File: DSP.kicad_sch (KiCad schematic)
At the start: 26 parts, among them J2 Conn_01x04, J3 Conn_01x04, J4 MEM2067-02-180-00-A_REVB, J6 Conn_01x04, U4 STM32F401RBTx, U5 23K256, Y1 16MHz

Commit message: modifications for rev 3
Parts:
- removed C28: 100n, Capacitor_SMD:C_0603_1608Metric_Pad1.08x0.95mm_HandSolder, symbol Device:C_Small
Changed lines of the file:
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@@
 (kicad_sch (version 20230121) (generator eeschema)
   (paper "A4")
-  (junction (at 53.34 154.94) (diameter 0) (color 0 0 0 0)
-  )
   (junction (at 114.3 34.29) (diameter 0) (color 0 0 0 0)
   )
@@
   (junction (at 167.64 34.29) (diameter 0) (color 0 0 0 0)
   )
+  (junction (at 67.31 177.8) (diameter 0) (color 0 0 0 0)
+  )
   (junction (at 140.97 90.17) (diameter 0) (color 0 0 0 0)
   )
@@
   (junction (at 185.42 110.49) (diameter 0) (color 0 0 0 0)
   )
-  (junction (at 53.34 177.8) (diameter 0) (color 0 0 0 0)
-  )
   (junction (at 111.76 128.27) (diameter 0) (color 0 0 0 0)
-  )
-  (junction (at 53.34 172.72) (diameter 0) (color 0 0 0 0)
   )
   (junction (at 66.04 87.63) (diameter 0) (color 0 0 0 0)
@@
     (stroke (width 0) (type default))
   )
-  (wire (pts (xy 53.34 167.64) (xy 53.34 172.72))
-    (stroke (width 0) (type default))
-  )
   (wire (pts (xy 111.76 125.73) (xy 111.76 128.27))
     (stroke (width 0) (type default))
@@
     (stroke (width 0) (type default))
   )
+  (wire (pts (xy 67.31 152.4) (xy 67.31 154.94))
+    (stroke (width 0) (type default))
+  )
   (wire (pts (xy 60.96 74.93) (xy 66.04 74.93))
     (stroke (width 0) (type default))
@@
     (stroke (width 0) (type default))
   )
+  (wire (pts (xy 67.31 154.94) (xy 69.85 154.94))
+    (stroke (width 0) (type default))
+  )
   (wire (pts (xy 185.42 118.11) (xy 185.42 120.65))
     (stroke (width 0) (type default))
@@
     (stroke (width 0) (type default))
   )
-  (wire (pts (xy 53.34 177.8) (xy 53.34 179.07))
-    (stroke (width 0) (type default))
-  )
   (wire (pts (xy 157.48 43.18) (xy 157.48 44.45))
     (stroke (width 0) (type default))
@@
     (stroke (width 0) (type default))
   )
-  (wire (pts (xy 53.34 177.8) (xy 69.85 177.8))
-    (stroke (width 0) (type default))
-  )
   (wire (pts (xy 172.72 34.29) (xy 177.8 34.29))
     (stroke (width 0) (type default))
@@
     (stroke (width 0) (type default))
   )
+  (wire (pts (xy 67.31 172.72) (xy 67.31 177.8))
+    (stroke (width 0) (type default))
+  )
   (wire (pts (xy 214.63 130.81) (xy 215.9 130.81))
     (stroke (width 0) (type default))
@@
     (stroke (width 0) (type default))
   )
+  (wire (pts (xy 67.31 177.8) (xy 67.31 180.34))
+    (stroke (width 0) (type default))
+  )
   (wire (pts (xy 111.76 128.27) (xy 114.3 128.27))
     (stroke (width 0) (type default))
@@
     (stroke (width 0) (type default))
   )
+  (wire (pts (xy 69.85 172.72) (xy 67.31 172.72))
+    (stroke (width 0) (type default))
+  )
   (wire (pts (xy 142.24 90.17) (xy 140.97 90.17))
     (stroke (width 0) (type default))
@@
     (stroke (width 0) (type default))
   )
+  (wire (pts (xy 67.31 177.8) (xy 69.85 177.8))
+    (stroke (width 0) (type default))
+  )
   (wire (pts (xy 140.97 96.52) (xy 140.97 97.79))
     (stroke (width 0) (type default))
@@
     (stroke (width 0) (type default))
   )
-  (wire (pts (xy 53.34 172.72) (xy 53.34 177.8))
-    (stroke (width 0) (type default))
-  )
   (wire (pts (xy 54.61 34.29) (xy 54.61 36.83))
     (stroke (width 0) (type default))
@@
     (stroke (width 0) (type default))
   )
-  (wire (pts (xy 53.34 172.72) (xy 69.85 172.72))
-    (stroke (width 0) (type default))
-  )
   (wire (pts (xy 182.88 38.1) (xy 182.88 34.29))
     (stroke (width 0) (type default))
@@
     (stroke (width 0) (type default))
   )
-  (wire (pts (xy 53.34 154.94) (xy 69.85 154.94))
-    (stroke (width 0) (type default))
-  )
   (wire (pts (xy 172.72 38.1) (xy 172.72 34.29))
     (stroke (width 0) (type default))
@@
     (stroke (width 0) (type default))
   )
-  (wire (pts (xy 53.34 152.4) (xy 53.34 154.94))
-    (stroke (width 0) (type default))
-  )
   (wire (pts (xy 214.63 123.19) (xy 215.9 123.19))
     (stroke (width 0) (type default))
@@
   )
   (wire (pts (xy 119.38 34.29) (xy 119.38 36.83))
-    (stroke (width 0) (type default))
-  )
-  (wire (pts (xy 53.34 154.94) (xy 53.34 162.56))
     (stroke (width 0) (type default))
   )
@@
     )
   )
-  (symbol (lib_id "power:GND") (at 53.34 179.07 0) (unit 1)
+  (symbol (lib_id "power:GND") (at 67.31 180.34 0) (unit 1)
     (in_bom yes) (on_board yes) (dnp no)
-    (property "Reference" "#PWR056" (at 53.34 185.42 0)
-      (effects (font (size 1.27 1.27)) hide)
-    )
-    (property "Value" "GND" (at 53.34 182.88 0)
-      (effects (font (size 1.27 1.27)))
-    )
-    (property "Footprint" "" (at 53.34 179.07 0)
-      (effects (font (size 1.27 1.27)) hide)
-    )
-    (property "Datasheet" "" (at 53.34 179.07 0)
+    (property "Reference" "#PWR056" (at 67.31 186.69 0)
+      (effects (font (size 1.27 1.27)) hide)
+    )
+    (property "Value" "GND" (at 67.31 184.15 0)
+      (effects (font (size 1.27 1.27)))
+    )
+    (property "Footprint" "" (at 67.31 180.34 0)
+      (effects (font (size 1.27 1.27)) hide)
+    )
+    (property "Datasheet" "" (at 67.31 180.34 0)
       (effects (font (size 1.27 1.27)) hide)
     )
@@
         (path "/e63e39d7-6ac0-4ffd-8aa3-1841a4541b55/65c41d2a-7921-40f6-8a66-43d43155f96a"
           (reference "#PWR035") (unit 1)
-        )
-      )
-    )
-  )
-  (symbol (lib_id "Device:C_Small") (at 53.34 165.1 0) (unit 1)
-    (in_bom yes) (on_board yes) (dnp no)
-    (property "Reference" "C28" (at 54.61 163.83 0)
-      (effects (font (size 1.27 1.27)) (justify left))
-    )
-    (property "Value" "100n" (at 54.61 166.37 0)
-      (effects (font (size 1.27 1.27)) (justify left))
-    )
-    (property "Footprint" "Capacitor_SMD:C_0603_1608Metric_Pad1.08x0.95mm_HandSolder" (at 53.34 165.1 0)
-      (effects (font (size 1.27 1.27)) hide)
-    )
-    (property "Datasheet" "~" (at 53.34 165.1 0)
-      (effects (font (size 1.27 1.27)) hide)
-    )
-    (pin "1")
-    (pin "2")
-    (instances
-      (project "Apollo - DSP"
-        (path "/e63e39d7-6ac0-4ffd-8aa3-1841a4541b55/65c41d2a-7921-40f6-8a66-43d43155f96a"
-          (reference "C28") (unit 1)
         )
       )
@@
     )
   )
-  (symbol (lib_id "power:+3.3V") (at 53.34 152.4 0) (unit 1)
-    (in_bom yes) (on_board yes) (dnp no) (fields_autoplaced)
-    (property "Reference" "#PWR055" (at 53.34 156.21 0)
-      (effects (font (size 1.27 1.27)) hide)
-    )
-    (property "Value" "+3.3V" (at 53.34 147.32 0)
-      (effects (font (size 1.27 1.27)))
-    )
-    (property "Footprint" "" (at 53.34 152.4 0)
-      (effects (font (size 1.27 1.27)) hide)
-    )
-    (property "Datasheet" "" (at 53.34 152.4 0)
-      (effects (font (size 1.27 1.27)) hide)
-    )
+  (symbol (lib_id "power:+3.3V") (at 67.31 152.4 0) (unit 1)
+    (in_bom yes) (on_board yes) (dnp no) (fields_autoplaced)
+    (property "Reference" "#PWR055" (at 67.31 156.21 0)
+      (effects (font (size 1.27 1.27)) hide)
+    )
+    (property "Value" "+3.3V" (at 67.31 147.32 0)
+      (effects (font (size 1.27 1.27)))
+    )
+    (property "Footprint" "" (at 67.31 152.4 0)
+      (effects (font (size 1.27 1.27)) hide)
+    )
+    (property "Datasheet" "" (at 67.31 152.4 0)
+      (effects (font (size 1.27 1.27)) hide)
+    )

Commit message: ready for order
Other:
- moved on the sheet: R?
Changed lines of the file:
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@@
   (junction (at 185.42 110.49) (diameter 0) (color 0 0 0 0)
+  )
+  (junction (at 82.55 46.99) (diameter 0) (color 0 0 0 0)
   )
   (junction (at 111.76 128.27) (diameter 0) (color 0 0 0 0)
@@
     (stroke (width 0) (type default))
   )
-  (wire (pts (xy 36.83 40.64) (xy 39.37 40.64))
+  (wire (pts (xy 82.55 46.99) (xy 81.28 46.99))
     (stroke (width 0) (type default))
   )
@@
     (stroke (width 0) (type default))
   )
-  (wire (pts (xy 36.83 43.18) (xy 36.83 40.64))
+  (wire (pts (xy 82.55 49.53) (xy 82.55 46.99))
     (stroke (width 0) (type default))
   )
@@
     (stroke (width 0) (type default))
   )
+  (wire (pts (xy 82.55 46.99) (xy 96.52 46.99))
+    (stroke (width 0) (type default))
+  )
   (wire (pts (xy 54.61 36.83) (xy 60.96 36.83))
     (stroke (width 0) (type default))
@@
     (stroke (width 0) (type default))
   )
-  (wire (pts (xy 36.83 48.26) (xy 36.83 49.53))
+  (wire (pts (xy 82.55 54.61) (xy 82.55 55.88))
     (stroke (width 0) (type default))
   )
@@
     (stroke (width 0) (type default))
   )
-  (global_label "BOOT0" (shape input) (at 39.37 40.64 0) (fields_autoplaced)
-    (effects (font (size 1 1)) (justify left))
-    (property "Intersheetrefs" "${INTERSHEET_REFS}" (at 46.0795 40.5775 0)
-      (effects (font (size 1 1)) (justify left) hide)
-    )
-  )
-  (global_label "BOOT0" (shape input) (at 96.52 46.99 180) (fields_autoplaced)
+  (global_label "BOOT0" (shape input) (at 81.28 46.99 180) (fields_autoplaced)
     (effects (font (size 1 1)) (justify right))
-    (property "Intersheetrefs" "${INTERSHEET_REFS}" (at 89.8105 46.9275 0)
+    (property "Intersheetrefs" "${INTERSHEET_REFS}" (at 74.1202 46.99 0)
       (effects (font (size 1 1)) (justify right) hide)
     )
@@
     )
   )
-  (symbol (lib_id "power:GND") (at 36.83 49.53 0) (unit 1)
-    (in_bom yes) (on_board yes) (dnp no) (fields_autoplaced)
-    (property "Reference" "#PWR?" (at 36.83 55.88 0)
-      (effects (font (size 1.27 1.27)) hide)
-    )
-    (property "Value" "GND" (at 36.83 54.61 0)
-      (effects (font (size 1.27 1.27)))
-    )
-    (property "Footprint" "" (at 36.83 49.53 0)
-      (effects (font (size 1.27 1.27)) hide)
-    )
-    (property "Datasheet" "" (at 36.83 49.53 0)
+  (symbol (lib_id "power:GND") (at 82.55 55.88 0) (unit 1)
+    (in_bom yes) (on_board yes) (dnp no)
+    (property "Reference" "#PWR?" (at 82.55 62.23 0)
+      (effects (font (size 1.27 1.27)) hide)
+    )
+    (property "Value" "GND" (at 82.55 59.69 0)
+      (effects (font (size 1.27 1.27)))
+    )
+    (property "Footprint" "" (at 82.55 55.88 0)
+      (effects (font (size 1.27 1.27)) hide)
+    )
+    (property "Datasheet" "" (at 82.55 55.88 0)
       (effects (font (size 1.27 1.27)) hide)
     )
@@
     )
   )
-  (symbol (lib_id "Device:R_Small") (at 36.83 45.72 0) (unit 1)
-    (in_bom yes) (on_board yes) (dnp no)
-    (property "Reference" "R?" (at 38.1 44.45 0)
-      (effects (font (size 1.27 1.27)) (justify left))
-    )
-    (property "Value" "10k" (at 38.1 46.99 0)
-      (effects (font (size 1.27 1.27)) (justify left))
-    )
-    (property "Footprint" "Resistor_SMD:R_0603_1608Metric_Pad0.98x0.95mm_HandSolder" (at 36.83 45.72 0)
-      (effects (font (size 1.27 1.27)) hide)
-    )
-    (property "Datasheet" "~" (at 36.83 45.72 0)
-      (effects (font (size 1.27 1.27)) hide)
-    )
+  (symbol (lib_id "Device:R_Small") (at 82.55 52.07 0) (unit 1)
+    (in_bom yes) (on_board yes) (dnp no)
+    (property "Reference" "R?" (at 83.82 50.8 0)
+      (effects (font (size 1.27 1.27)) (justify left))
+    )
+    (property "Value" "10k" (at 83.82 53.34 0)
+      (effects (font (size 1.27 1.27)) (justify left))
+    )
+    (property "Footprint" "Resistor_SMD:R_0603_1608Metric_Pad0.98x0.95mm_HandSolder" (at 82.55 52.07 0)
+      (effects (font (size 1.27 1.27)) hide)
+    )
+    (property "Datasheet" "~" (at 82.55 52.07 0)
+      (effects (font (size 1.27 1.27)) hide)
+    )

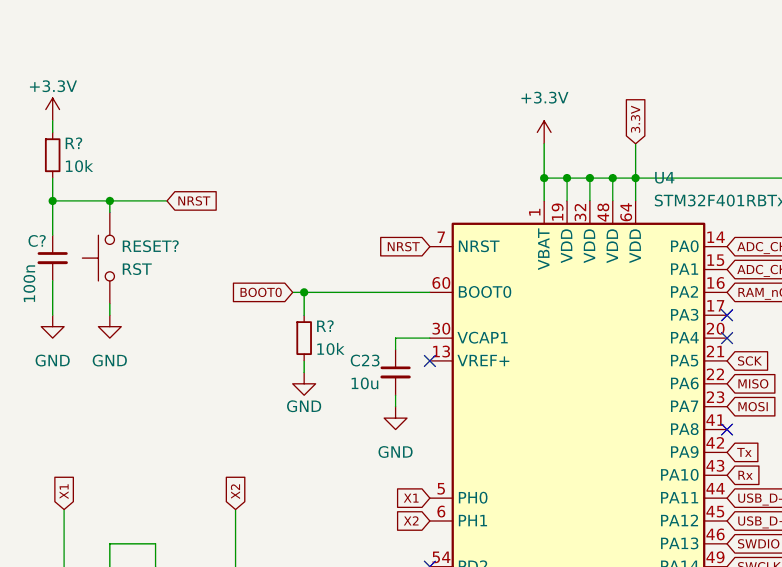
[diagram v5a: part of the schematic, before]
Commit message: FIXED ADCVOLTAGE PIN
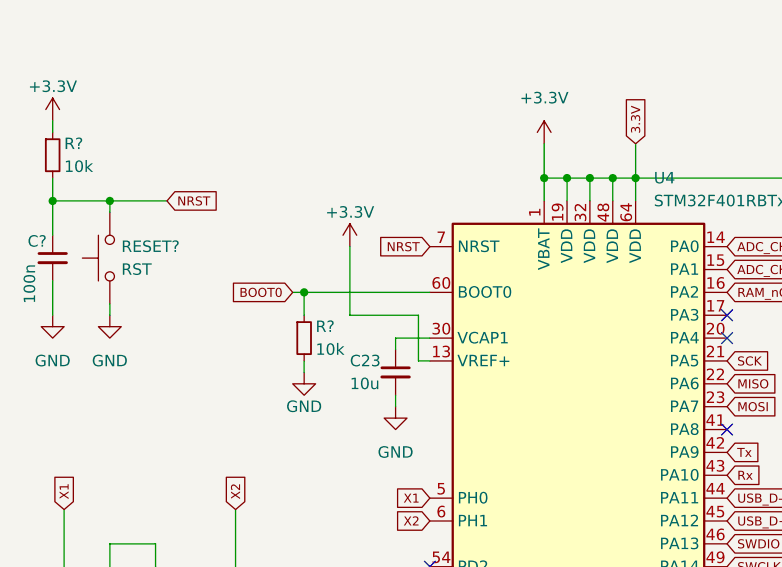
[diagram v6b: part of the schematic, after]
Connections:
- net +3V3: now also U4.13 (VREF+)
- no-connect marks 34 -> 33
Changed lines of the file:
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@@
   (no_connect (at 96.52 110.49))
   (no_connect (at 69.85 162.56))
-  (no_connect (at 96.52 54.61))
   (no_connect (at 129.54 107.95))
   (no_connect (at 129.54 52.07))
@@
     (stroke (width 0) (type default))
   )
+  (wire (pts (xy 95.25 54.61) (xy 96.52 54.61))
+    (stroke (width 0) (type default))
+  )
   (wire (pts (xy 54.61 45.72) (xy 54.61 49.53))
     (stroke (width 0) (type default))
@@
     (stroke (width 0) (type default))
   )
+  (wire (pts (xy 87.63 49.53) (xy 95.25 49.53))
+    (stroke (width 0) (type default))
+  )
   (wire (pts (xy 82.55 49.53) (xy 82.55 46.99))
     (stroke (width 0) (type default))
@@
     (stroke (width 0) (type default))
   )
+  (wire (pts (xy 95.25 49.53) (xy 95.25 54.61))
+    (stroke (width 0) (type default))
+  )
   (wire (pts (xy 157.48 43.18) (xy 157.48 44.45))
     (stroke (width 0) (type default))
@@
   )
   (wire (pts (xy 162.56 43.18) (xy 162.56 44.45))
+    (stroke (width 0) (type default))
+  )
+  (wire (pts (xy 87.63 41.91) (xy 87.63 49.53))
     (stroke (width 0) (type default))
   )
@@
         )
       )
+    )
+  )
+  (symbol (lib_id "power:+3.3V") (at 87.63 41.91 0) (unit 1)
+    (in_bom yes) (on_board yes) (dnp no)
+    (property "Reference" "#PWR?" (at 87.63 45.72 0)
+      (effects (font (size 1.27 1.27)) hide)
+    )
+    (property "Value" "+3.3V" (at 87.63 38.1 0)
+      (effects (font (size 1.27 1.27)))
+    )
+    (property "Footprint" "" (at 87.63 41.91 0)
+      (effects (font (size 1.27 1.27)) hide)
+    )
+    (property "Datasheet" "" (at 87.63 41.91 0)
+      (effects (font (size 1.27 1.27)) hide)
+    )
+    (pin "1")
+    (instances
+      (project "STM32F103 devboard"
+        (path "/7cd8109f-5f99-46a5-9e32-14f7754144db"
+          (reference "#PWR?") (unit 1)
+        )
+      )
+      (project "Apollo - DSP"
+        (path "/e63e39d7-6ac0-4ffd-8aa3-1841a4541b55/65c41d2a-7921-40f6-8a66-43d43155f96a"
+          (reference "#PWR060") (unit 1)
+        )
+      )

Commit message: refreshing design
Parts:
- added TP1, TP2, TP3: TestPoint, TestPoint:TestPoint_Pad_D1.0mm, symbol Connector:TestPoint
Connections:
- net BOOT0: now also TP1.1
- net at U4.36 (PB15): now also TP3.1
- net at U4.39 (PC8): now also TP2.1
- no-connect marks 33 -> 31
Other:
- moved on the sheet: D2, R8, R?
